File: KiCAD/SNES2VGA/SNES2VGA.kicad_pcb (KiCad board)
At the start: 2 copper layers, 30.8 x 23.6 mm, 17 parts, among them J1 3.5mm_vertical, P1 AVMulti_Main, P2 VGA

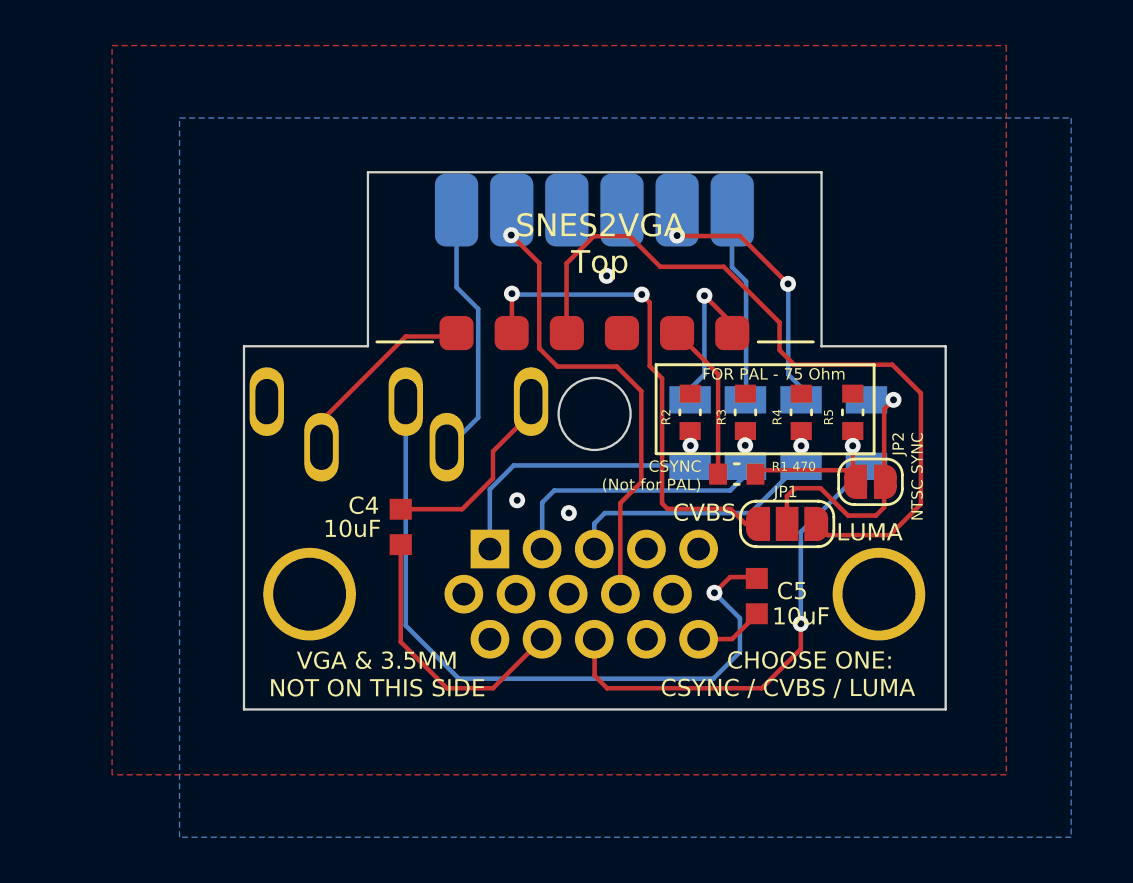
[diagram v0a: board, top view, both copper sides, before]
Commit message: Update to KiCad 9
 - Use kicad symbols and footprints if possible
 - Add JLCPCB QR/number placement square/text
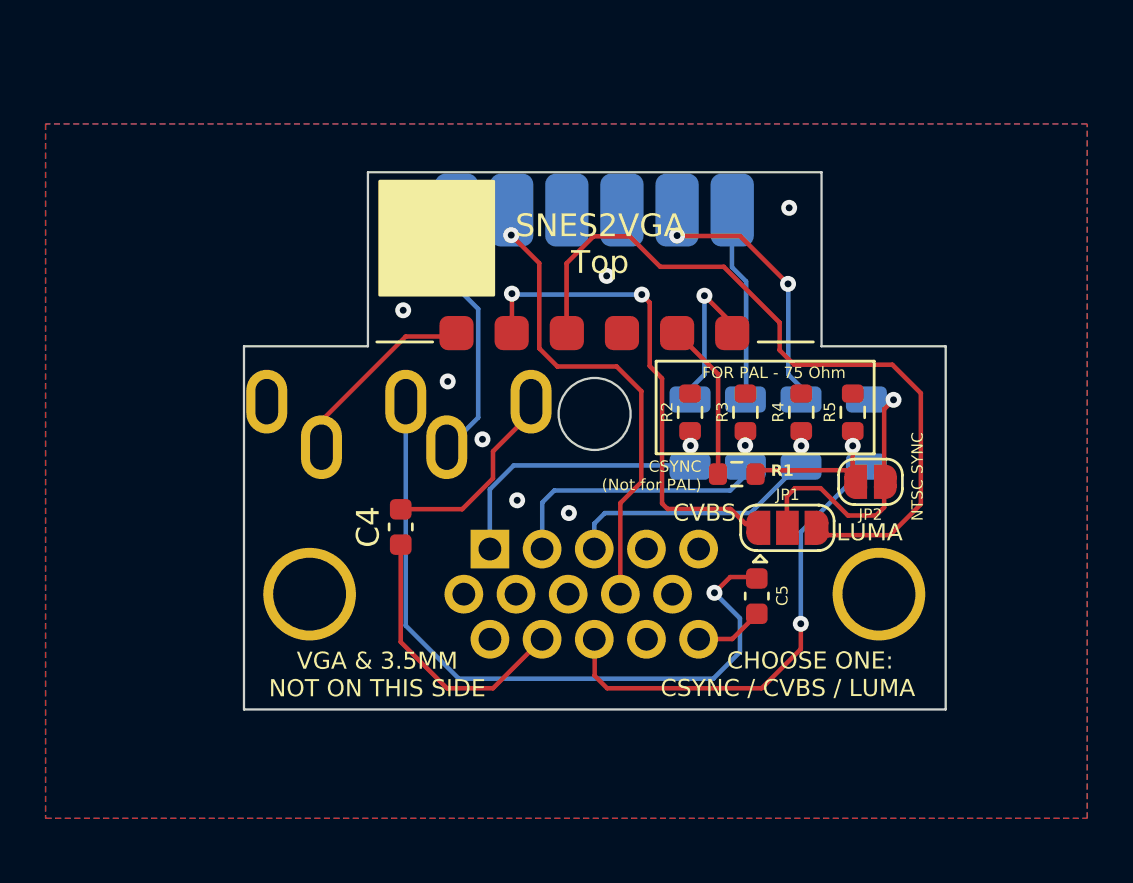
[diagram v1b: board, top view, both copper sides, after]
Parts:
- removed G***: LOGO, SNES2VGA_Library:Outline_PCB_Main
- C1, C2, C3, C6: footprint SNES2VGA_Library:Cap_SMD_1206 -> Capacitor_SMD:C_1206_3216Metric
- C4, C5: footprint SNES2VGA_Library:Cap_SMD_0603 -> Capacitor_SMD:C_0603_1608Metric
- J1: value 3.5mm_vertical -> AudioJack3_SwitchTR; footprint SNES2VGA_Library:3.5mm_vertical -> Connector_Audio:Jack_3.5mm_CUI_SJ1-3535NG_Horizontal
- JP1: footprint SNES2VGA_Library:SolderJumper-3_P1.3mm_Open_RoundedPad1.0x1.5mm -> Jumper:SolderJumper-3_P1.3mm_Open_RoundedPad1.0x1.5mm
- R1, R2, R3, R4, R5: footprint SNES2VGA_Library:Resistor_SMD_0603 -> Resistor_SMD:R_0603_1608Metric
- moved JP1 0.17 mm to (149.4, 104.1)
- turned C4 to 90 degrees
- turned C5 to 90 degrees
- turned J1 to -90 degrees
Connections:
- C4 pad 1: /Audio_L_from_Jack -> /Audio_L_to_VGA
- C4 pad 2: /Audio_L_to_VGA -> /Audio_L_from_Jack
- C5 pad 1: /Audio_R_from_Jack -> /Audio_R_to_VGA
- C5 pad 2: /Audio_R_to_VGA -> /Audio_R_from_Jack
- P2 pad 14: /VSYNC_VGA -> unconnected-(P2-VSYNC-Pad14)
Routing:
- net /Green_SNES: track 8.22 -> 7.36 mm
- net /Green_VGA: track 13.5 -> 12.7 mm
- net /HSYNC_VGA: track 27.5 -> 26.9 mm
- net /Audio_R_SNES: track 11.4 -> 10.8 mm
- net /Red_SNES: track 6.84 -> 6.32 mm
- net /Audio_L_from_Jack: track 8.71 -> 8.20 mm
- net GND: vias 3 -> 7
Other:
- rule pad_to_mask_clearance: 0.0508 -> 0
